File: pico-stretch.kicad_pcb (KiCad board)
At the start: 4 copper layers, 84.8 x 23.7 mm, 68 parts, among them J1 Conn_01x32_MountingPin, J2 Conn_01x03_Pin, J3 Conn_01x32_MountingPin, U4 Winbond W25Q128JVSIQ, U5 RPI Radio Module 2, U6 ESP-PSRAM32

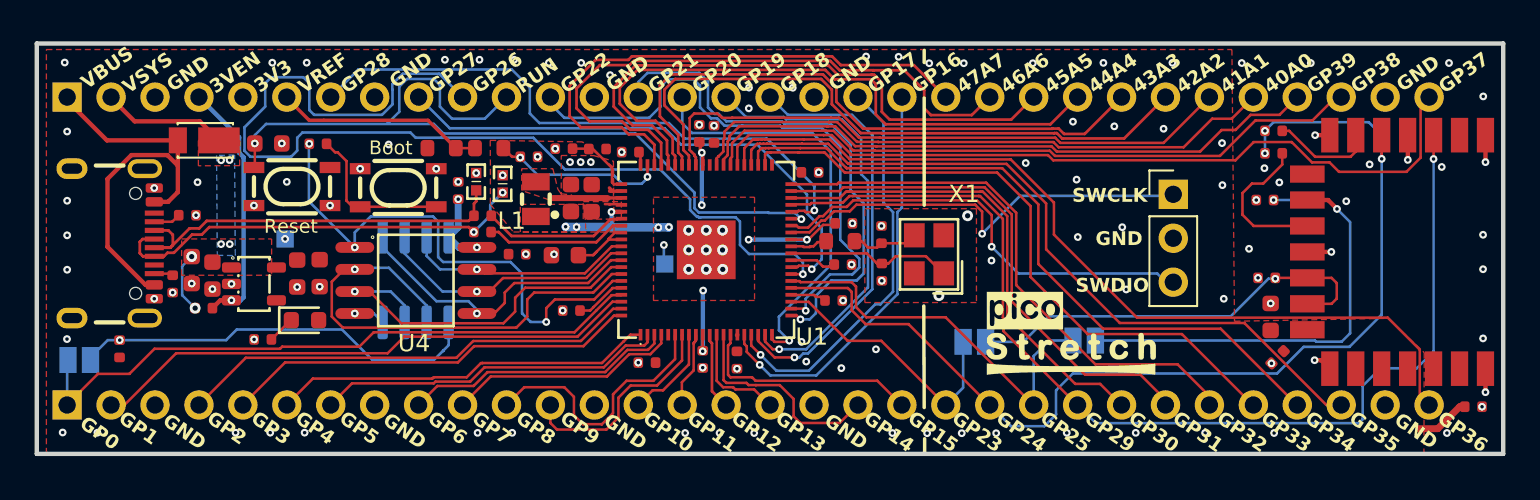
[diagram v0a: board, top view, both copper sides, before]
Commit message: Major re-work for castellated pads and PSRAM on top
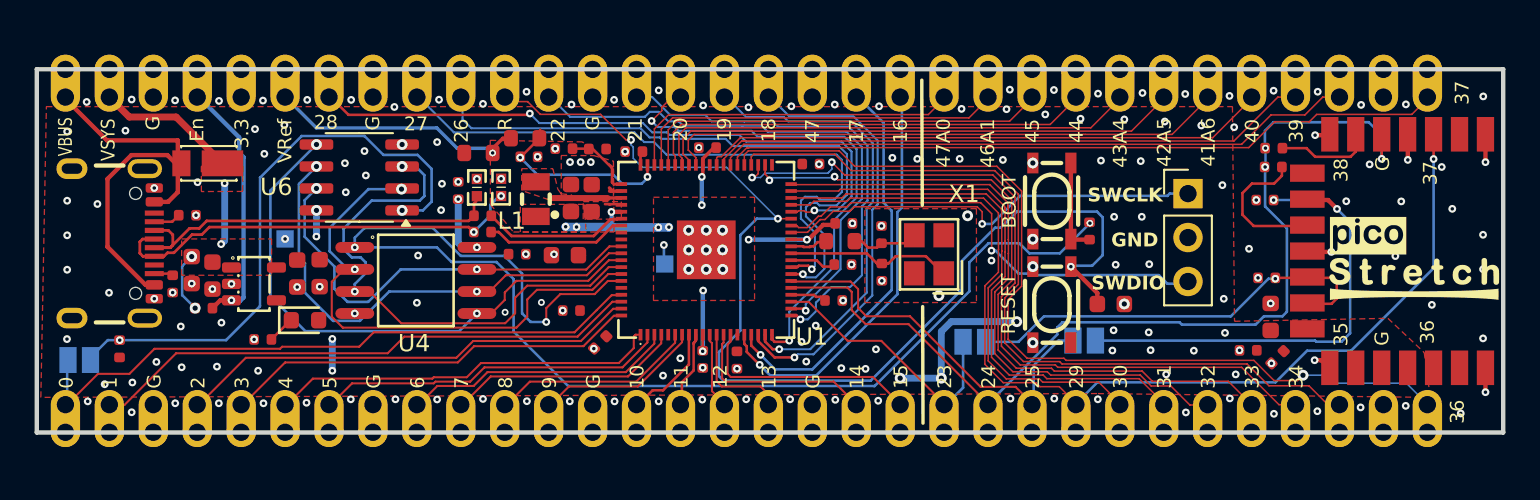
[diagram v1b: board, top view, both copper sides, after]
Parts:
- removed C14: 100nF, PCM_JLCPCB:C_0402
- removed J1, J3: Conn_01x32_MountingPin, Connector_PinHeader_2.54mm:PinHeader_1x32_P2.54mm_Vertical
- added J4: Conn_01x64_Castellated_Pads, Castellated:Castellated_Pad_64, F.Cu at (110.8, 92.6)
- U6: moved to F.Cu
- moved C15 49.6 mm to (171.2, 104.6)
- moved R5 44.9 mm to (170.0, 100.3), turned to 90 degrees
- moved Reset1 44.5 mm to (167.8, 104.6), turned to -90 degrees
- moved Boot1 37.8 mm to (167.8, 98.6), turned to -90 degrees
- moved G*** 20.3 mm to (187.3, 102.9)
- moved C21 13.4 mm to (179.2, 107.2), turned to 180 degrees
- moved U6 6.75 mm to (127.8, 97.2), turned to 180 degrees
- moved C1 2.94 mm to (141.7, 106.8), turned to -135 degrees
- moved R7 2.16 mm to (137.4, 95.0)
- moved R8 2.15 mm to (134.7, 95.8)
- moved D1 1.35 mm to (118.7, 96.4)
- moved R15 1.00 mm to (180.7, 95.5)
- moved C13 0.95 mm to (147.9, 95.5), turned to 0 degrees
- moved J2 0.85 mm to (175.7, 98.2)
- moved R16 0.79 mm to (180.6, 96.6)
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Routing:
- net Net-(U1-QSPI_SS): track 30.3 -> 74.3 mm
- net GPIO26: track 59.1 -> 35.7 mm
- net RUN: track 48.5 -> 65.6 mm, vias 2 -> 3
- net QSPI_SD0: track 17.6 -> 32.8 mm, vias 1 -> 2
- net GPIO46/ADC6: track 35.1 -> 21.8 mm
- net QSPI_SCLK: track 15.2 -> 28.3 mm, vias 1 -> 2
- net GPIO47/ADC7: track 31.9 -> 19.7 mm
- net QSPI_SD3: track 13.3 -> 25.0 mm, vias 1 -> 2
- net Net-(JP1-A): track 24.2 -> 34.4 mm, vias 1 -> 2
- net GPIO44/ADC4: track 36.3 -> 26.1 mm
- net GPIO45/ADC5: track 34.1 -> 23.9 mm
- net QSPI_SD2: track 22.1 -> 30.9 mm, vias 1 -> 2
- net GPIO43/ADC3: track 34.9 -> 28.3 mm
- net GPIO42/ADC2: track 37.1 -> 30.5 mm
- net GPIO24: track 61.9 -> 55.8 mm
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- removed copper zone on B.Cu, net VSYS
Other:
- board size 84.8 x 23.7 mm -> 84.8 x 21 mm
- board text added: "0"
- board text added: "1"
- board text added: "10"
- board text added: "11"
- board text added: "12"
- board text added: "13"
- board text added: "14"
- board text added: "15"
- board text added: "16"
- board text added: "17"
- board text added: "18"
- board text added: "19"
- board text added: "2"
- board text added: "20"
- board text added: "21"
- board text added: "22"
- board text added: "23"
- board text added: "24"
- board text added: "25"
- board text added: "26"
- board text added: "27"
- board text added: "28"
- board text added: "29"
- board text added: "3"
- board text added: "3.3"
- board text added: "30"
- board text added: "31"
- board text added: "32"
- board text added: "33"
- board text added: "34"
- board text added: "35"
- board text added: "36"
- board text added: "37"
- board text added: "38"
- board text added: "39"
- board text added: "4"
- board text added: "40"
- board text added: "41A6"
- board text added: "42A5"
- board text added: "43A4"
- board text added: "44"
- board text added: "45"
- board text added: "46A1"
- board text added: "47"
- board text added: "47A0"
- board text added: "5"
- board text added: "6"
- board text added: "7"
- board text added: "8"
- board text added: "9"
- board text added: "BOOT"
- board text added: "En"
- board text added: "G"
- board text added: "R"
- board text added: "RESET"
- board text added: "VRef"
- board text removed: "3V3"
- board text removed: "3VEN"
- board text removed: "40A0"
- board text removed: "41A1"
- board text removed: "42A2"
- board text removed: "43A3"
- board text removed: "44A4"
- board text removed: "45A5"
- board text removed: "46A6"
- board text removed: "47A7"
- board text removed: "Boot"
- board text removed: "GP0"
- board text removed: "GP1"
- board text removed: "GP10"
- board text removed: "GP11"
- board text removed: "GP12"
- board text removed: "GP13"
- board text removed: "GP14"
- board text removed: "GP15"
- board text removed: "GP16"
- board text removed: "GP17"
- board text removed: "GP18"
- board text removed: "GP19"
- board text removed: "GP2"
- board text removed: "GP20"
- board text removed: "GP21"
- board text removed: "GP22"
- board text removed: "GP23"
- board text removed: "GP24"
- board text removed: "GP25"
- board text removed: "GP26"
- board text removed: "GP27"
- board text removed: "GP28"
- board text removed: "GP29"
- board text removed: "GP3"
- board text removed: "GP30"
- board text removed: "GP31"
- board text removed: "GP32"
- board text removed: "GP33"
- board text removed: "GP34"
- board text removed: "GP35"
- board text removed: "GP36"
- board text removed: "GP37"
- board text removed: "GP38"
- board text removed: "GP39"
- board text removed: "GP4"
- board text removed: "GP5"
- board text removed: "GP6"
- board text removed: "GP7"
- board text removed: "GP8"
- board text removed: "GP9"
- board text removed: "RUN"
- board text removed: "Reset"
- board text removed: "VREF"

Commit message: Going to prod
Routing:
- net Net-(U1-QSPI_SS): track 74.3 -> 60.8 mm
- net GPIO37: track 42.0 -> 46.4 mm
- net GPIO38: track 37.1 -> 38.2 mm
- net 3V3: track 23.5 -> 24.5 mm, vias 10 -> 12
- net GPIO39: track 35.0 -> 35.9 mm
- net SWDIO: track 26.8 -> 27.6 mm
- net GPIO40/ADC0: track 33.0 -> 33.7 mm
- net GPIO36: track 53.3 -> 52.6 mm
- net QSPI_SD1: track 31.1 -> 30.5 mm
- net GPIO35: track 47.0 -> 46.4 mm
- net QSPI_SD2: track 30.9 -> 30.3 mm
- net GND: vias 199 -> 204

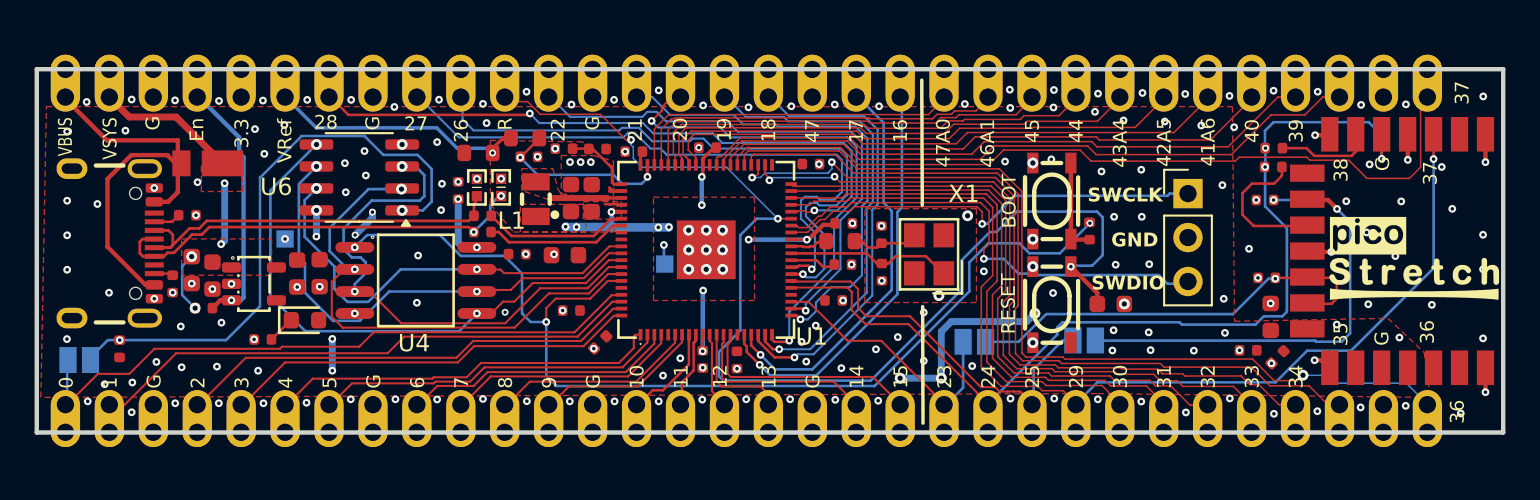
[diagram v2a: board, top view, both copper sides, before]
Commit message: Updated labels and production files
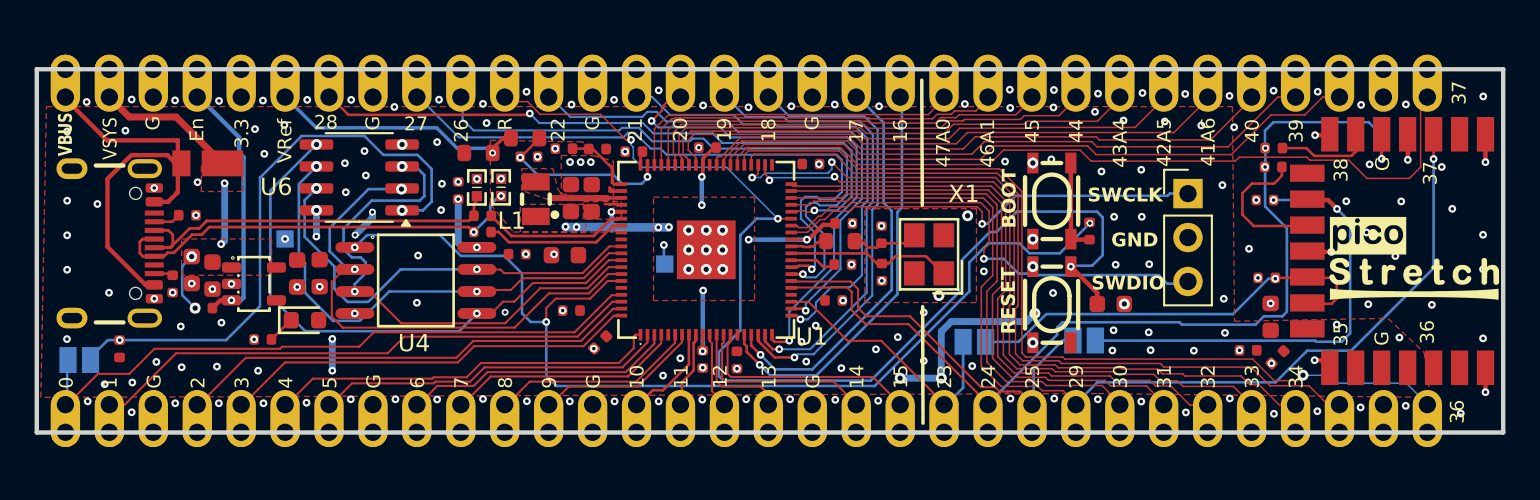
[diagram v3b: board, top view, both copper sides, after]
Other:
- board text removed: "47"
